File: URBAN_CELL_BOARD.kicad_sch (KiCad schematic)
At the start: 18 parts, among them J1 Conn_02x09_Odd_Even, J2 Conn_01x01_Female, J3 Conn_01x02_Female, J4 Conn_01x01_Female

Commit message: start adding power element
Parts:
- removed J3: Conn_01x02_Female, TerminalBlock_TE-Connectivity:TE_1986660-2, symbol Connector:Conn_01x02_Female
- added MP1, MP2: WP-SHFU, symbol WP-SHFU:WP-SHFU
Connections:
- net +48V: now also MP1.1
- net GND: now also MP2.1

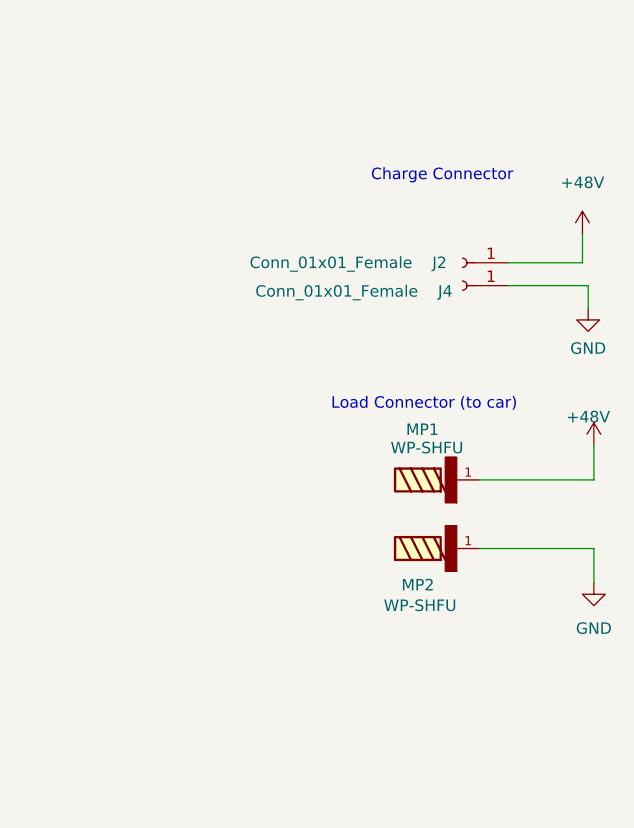
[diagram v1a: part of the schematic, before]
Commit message: Created charge conn footprints. Updated main conn footprints. Assigned 3D models to charge and main conn. Changed charge conn symbols. Updated datasheets. Consolidated custom footprints back into correct .pretty folder. Updated PCB from schematic BUT did NOT make actual changes to layout
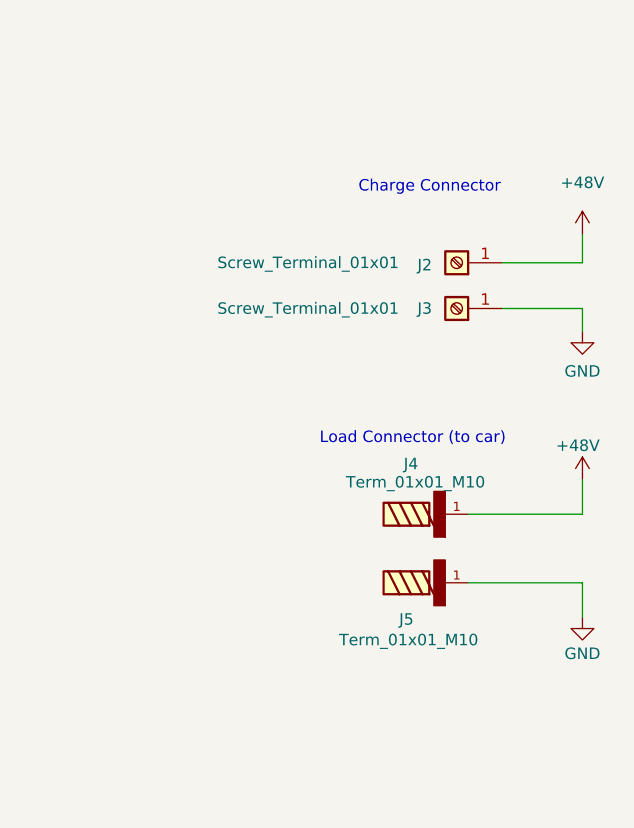
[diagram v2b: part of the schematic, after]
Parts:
- J2: value Conn_01x01_Female -> Screw_Terminal_01x01; footprint Phoenix_1889262:1889262 -> URBAN_CELL_CUSTOM_footprints:MOLEX_01X01_BARRIER_BLOCK; symbol Connector:Conn_01x01_Female -> Connector:Screw_Terminal_01x01
- J3: renamed from J4; value Conn_01x01_Female -> Screw_Terminal_01x01; footprint Phoenix_1889262:1889262 -> URBAN_CELL_CUSTOM_footprints:MOLEX_01X01_BARRIER_BLOCK; symbol Connector:Conn_01x01_Female -> Connector:Screw_Terminal_01x01
- J4: renamed from MP1; value WP-SHFU -> Term_01x01_M10; footprint (none) -> URBAN_CELL_CUSTOM_footprints:WURTH_M10_36PIN_TERM_7461100; DATASHEET-URL https://www.we-online.com/redexpert/spec/7461100?ae -> (none)
- J5: renamed from MP2; value WP-SHFU -> Term_01x01_M10; footprint (none) -> URBAN_CELL_CUSTOM_footprints:WURTH_M10_36PIN_TERM_7461100; DATASHEET-URL https://www.we-online.com/redexpert/spec/7461100?ae -> (none)
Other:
- moved on the sheet: J4, J5

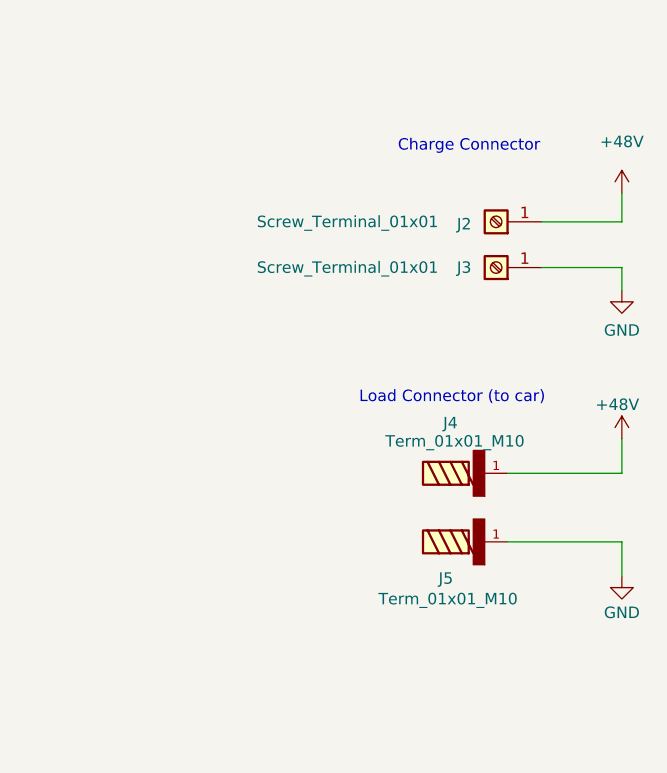
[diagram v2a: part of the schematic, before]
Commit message: Replaced load and charge connectors with new parts
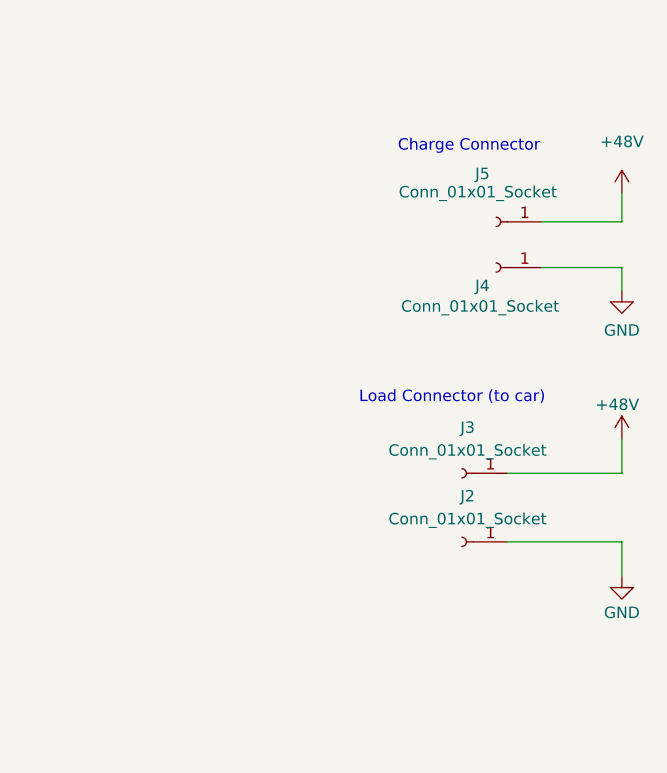
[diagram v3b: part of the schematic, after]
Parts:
- removed J2, J3: Screw_Terminal_01x01, URBAN_CELL_CUSTOM_footprints:MOLEX_01X01_BARRIER_BLOCK, symbol Connector:Screw_Terminal_01x01
- removed J4, J5: Term_01x01_M10, URBAN_CELL_CUSTOM_footprints:WURTH_M10_36PIN_TERM_7461100, symbol WP-SHFU:WP-SHFU
- added J2, J3: Conn_01x01_Socket, URBAN_CELL_CUSTOM_footprints:AMP_01x01_WTB036SV061250R_RADSOKPOWERLOK, symbol Connector:Conn_01x01_Socket
- added J4, J5: Conn_01x01_Socket, URBAN_CELL_CUSTOM_footprints:PHOENIX_01x01_1190362_TERMBLOCK_ANGLED, symbol Connector:Conn_01x01_Socket
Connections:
- net +48V: now also J3.1 (Pin_1), J5.1 (Pin_1)
- net GND: now also J2.1 (Pin_1), J4.1 (Pin_1)
